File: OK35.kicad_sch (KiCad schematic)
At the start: 74 parts, among them SW1 SW_SPST, SW10 SW_SPST, SW11 SW_SPST, SW12 SW_SPST, SW13 SW_SPST, SW14 SW_SPST, SW15 SW_SPST, SW16 SW_SPST, SW17 SW_SPST, SW18 SW_SPST, SW19 SW_SPST, SW2 SW_SPST, SW20 SW_SPST, SW21 SW_SPST, SW22 SW_SPST, SW23 SW_SPST, SW24 SW_SPST, SW25 SW_SPST, SW26 SW_SPST, SW27 SW_SPST, SW28 SW_SPST, SW29 SW_SPST, SW3 SW_SPST, SW30 SW_SPST, SW31 SW_SPST, SW32 SW_SPST, SW33 SW_SPST, SW34 SW_SPST, SW35 SW_SPST, SW4 SW_SPST, SW5 SW_SPST, SW6 SW_SPST, SW7 SW_SPST, SW8 SW_SPST, SW9 SW_SPST, U1 TRRS, U2 ProMicro

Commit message: Add files via upload
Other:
- moved on the sheet: D1, D10, D11, D12, D13, D14, D15, D16, D17, D18, D19, D2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

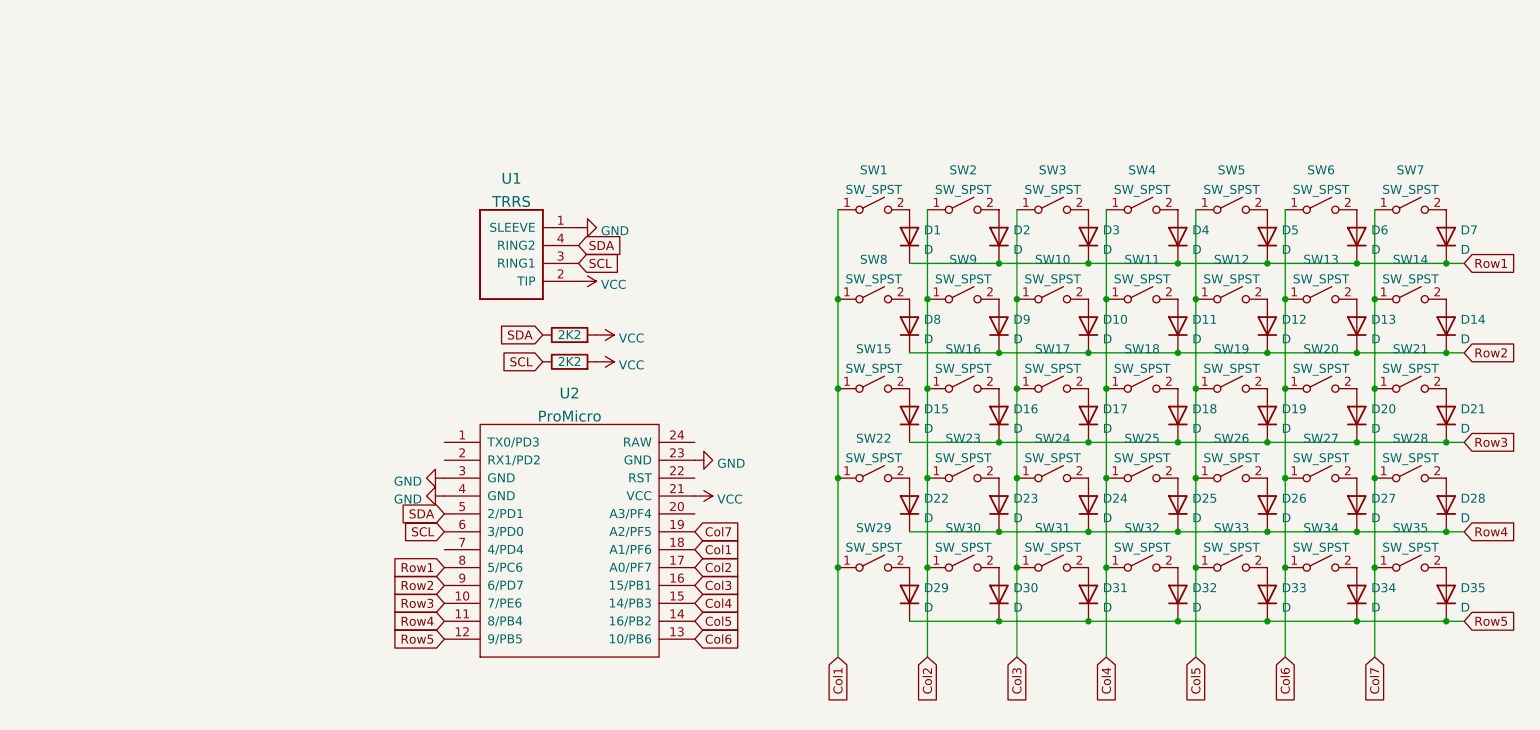
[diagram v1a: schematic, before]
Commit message: v0.1.1 - fixing noob mistakes
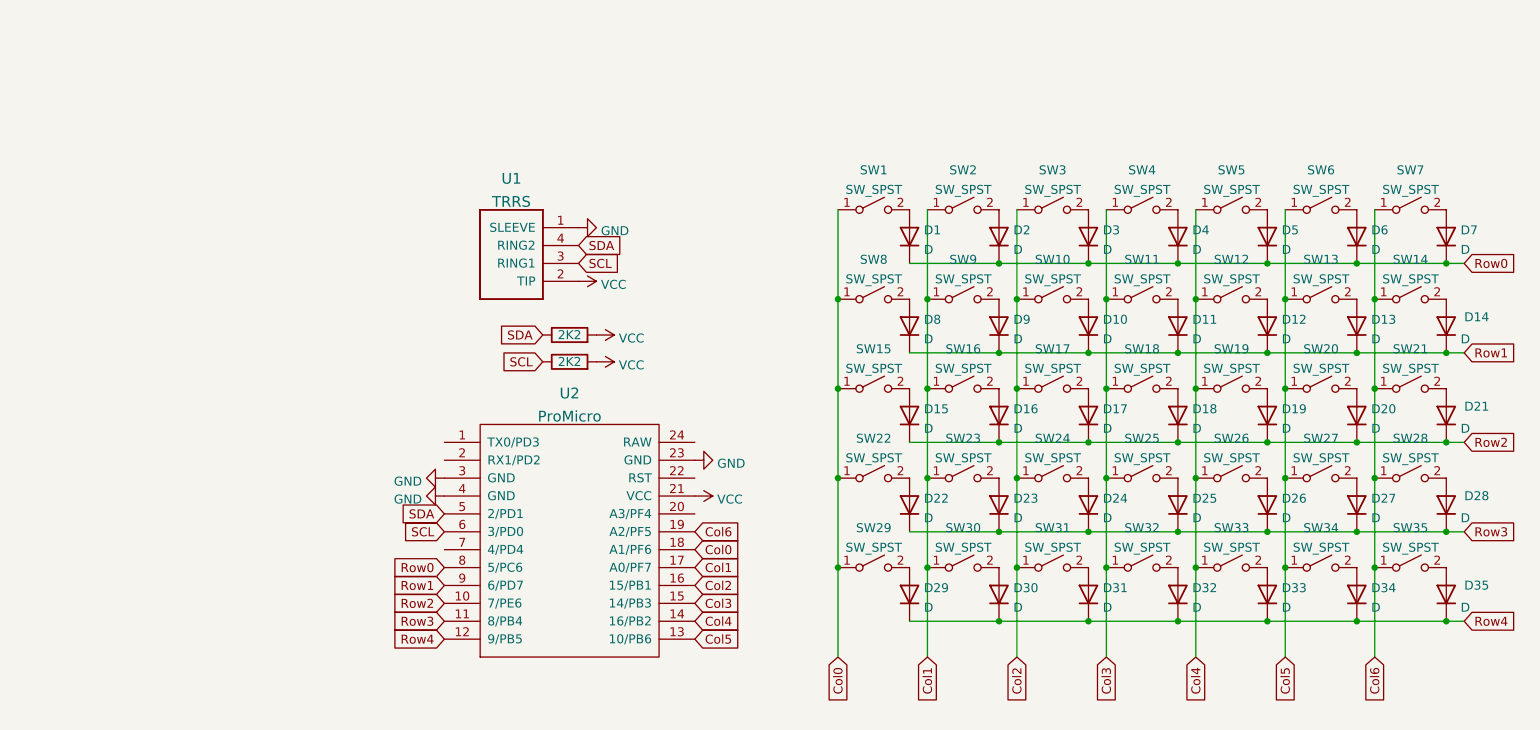
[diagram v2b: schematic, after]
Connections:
- net Col7 is gone; now on net Col6: SW14.1 (A), SW21.1 (A), SW28.1 (A), SW35.1 (A), SW7.1 (A), U2.19 (A2/PF5)
- net Row5 is gone; now on net Row4: D29.1 (K), D30.1 (K), D31.1 (K), D32.1 (K), D33.1 (K), D34.1 (K), D35.1 (K), U2.12 (9/PB5)
- net Col1: now also SW16.1 (A), SW2.1 (A), SW23.1 (A), SW30.1 (A), SW9.1 (A), U2.17 (A0/PF7); no longer SW1.1 (A), SW15.1 (A), SW22.1 (A), SW29.1 (A), SW8.1 (A), U2.18 (A1/PF6)
- net Col2: now also SW10.1 (A), SW17.1 (A), SW24.1 (A), SW3.1 (A), SW31.1 (A), U2.16 (15/PB1); no longer SW16.1 (A), SW2.1 (A), SW23.1 (A), SW30.1 (A), SW9.1 (A), U2.17 (A0/PF7)
- net Col3: now also SW11.1 (A), SW18.1 (A), SW25.1 (A), SW32.1 (A), SW4.1 (A), U2.15 (14/PB3); no longer SW10.1 (A), SW17.1 (A), SW24.1 (A), SW3.1 (A), SW31.1 (A), U2.16 (15/PB1)
- net Col4: now also SW12.1 (A), SW19.1 (A), SW26.1 (A), SW33.1 (A), SW5.1 (A), U2.14 (16/PB2); no longer SW11.1 (A), SW18.1 (A), SW25.1 (A), SW32.1 (A), SW4.1 (A), U2.15 (14/PB3)
- net Col5: now also SW13.1 (A), SW20.1 (A), SW27.1 (A), SW34.1 (A), SW6.1 (A), U2.13 (10/PB6); no longer SW12.1 (A), SW19.1 (A), SW26.1 (A), SW33.1 (A), SW5.1 (A), U2.14 (16/PB2)
- net Col6: no longer SW13.1 (A), SW20.1 (A), SW27.1 (A), SW34.1 (A), SW6.1 (A), U2.13 (10/PB6)
- net Row1: now also D10.1 (K), D11.1 (K), D12.1 (K), D13.1 (K), D14.1 (K), D8.1 (K), D9.1 (K), U2.9 (6/PD7); no longer D1.1 (K), D2.1 (K), D3.1 (K), D4.1 (K), D5.1 (K), D6.1 (K), D7.1 (K), U2.8 (5/PC6)
- net Row2: now also D15.1 (K), D16.1 (K), D17.1 (K), D18.1 (K), D19.1 (K), D20.1 (K), D21.1 (K), U2.10 (7/PE6); no longer D10.1 (K), D11.1 (K), D12.1 (K), D13.1 (K), D14.1 (K), D8.1 (K), D9.1 (K), U2.9 (6/PD7)
- net Row3: now also D22.1 (K), D23.1 (K), D24.1 (K), D25.1 (K), D26.1 (K), D27.1 (K), D28.1 (K), U2.11 (8/PB4); no longer D15.1 (K), D16.1 (K), D17.1 (K), D18.1 (K), D19.1 (K), D20.1 (K), D21.1 (K), U2.10 (7/PE6)
- net Row4: no longer D22.1 (K), D23.1 (K), D24.1 (K), D25.1 (K), D26.1 (K), D27.1 (K), D28.1 (K), U2.11 (8/PB4)
- new net Col0: SW1.1 (A), SW15.1 (A), SW22.1 (A), SW29.1 (A), SW8.1 (A), U2.18 (A1/PF6)
- new net Row0: D1.1 (K), D2.1 (K), D3.1 (K), D4.1 (K), D5.1 (K), D6.1 (K), D7.1 (K), U2.8 (5/PC6)

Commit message: cleanup some stuff
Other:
- company: (none) -> moth.monster
- title: (none) -> OK35
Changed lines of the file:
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@@
 (kicad_sch (version 20211123) (generator eeschema)
   (paper "A4")
+  (title_block
+    (title "OK35")
+    (date "2022-02-21")
+    (rev "0.1.1")
+    (company "moth.monster")
+  )
   (junction (at 139.7 63.5) (diameter 0) (color 0 0 0 0)
   )
